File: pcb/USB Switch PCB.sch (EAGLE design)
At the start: 36 parts, among them Q1 2N7002P, Q2 2N7002P, Q3 12 MHz, X1 AMPHENOL-0001LF, X2 UE27-USBA, X3 AMPHENOL-0001LF

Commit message: Starting to look good.
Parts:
- added R10, R11: 100Ω, rcl:R-EU_R0603
- added R7, R8, R9: 12kΩ, rcl:R-EU_R0603
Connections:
- new net GPIO15: MCU.GPIO15, R9.2
- new net GPIO2: MCU.GPIO2, R8.2
- new net N$3: MCU.GPIO5, R10.1
- new net N$5: MCU.GPIO4, R11.1
- net +5V: now also R7.1, R8.1
- net DATAGATE: now also R11.2; no longer MCU.GPIO5
- net GND: now also R9.1
- net GPIO0: now also R7.2
- net POWERGATE: now also R10.2; no longer MCU.GPIO4
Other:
- moved on the sheet: C1, C2, C7, MCU, R3, R4

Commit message: Converting everything
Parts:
- removed C3: 10µF, rcl:C-EUC0603
- removed C4: 100nF, rcl:C-EUC0603
- removed D3: BAS21LT1, USB Switch PCB:BAS40
- removed R5, R6: 470Ω, rcl:R-EU_R0603
- removed U$3: CH340G, ch340g:CH340G
- removed U$4: UMH3N, USB Switch PCB:UMH3N
- removed UIN: (no value), USB Switch PCB:FE05-1
- removed UOUT: (no value), USB Switch PCB:FE04-1
- removed X1, X3: AMPHENOL-0001LF, USB Switch PCB:AMPHENOL-0001LF
- added FLASH, RESET: MOMENTARY-SWITCH, USB Switch PCB:MOMENTARY-SWITCH
- added J1: (no value), SparkFun-Connectors:6_PIN_SERIAL_TARGET
- added U$6: USB-B, USB Switch PCB:USB-B
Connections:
- removed net D+ESP: U$3.D+, X3.D+
- removed net D-ESP: U$3.D-, X3.D-
- removed net DTR: U$3.DTR, U$4.BA, U$4.EB
- removed net ID: UIN.4, X1.ID
- removed net N$4: D3.A, X3.VCC
- removed net N$7: R5.2, U$3.TX
- removed net N$8: R6.2, U$3.RX
- removed net RTS: U$3.RTS, U$4.BB, U$4.EA
- new net ADC: MCU.ADC
- net +3V3: no longer C3.1, C4.1, U$3.VCC
- net +5V: now also J1.VCC; no longer D3.C, U$3.V3
- net D+I: now also U$6.D+; no longer UIN.3, X1.D+
- net D+O: no longer UOUT.3
- net D-I: now also U$6.D-; no longer UIN.2, X1.D-
- net D-O: no longer UOUT.2
- net GND: now also FLASH.P$2, J1.GND, RESET.P$2, U$6.GND; no longer C3.2, C4.2, U$3.GND, UIN.5, X1.GND, X3.GND
- net GNDO: no longer UOUT.4
- net GPIO0: now also FLASH.P$1; no longer U$4.CB
- net RST: now also RESET.P$1; no longer U$4.CA
- net RXD: now also J1.TXO; no longer R6.1
- net TXD: now also J1.RXI; no longer R5.1
- net VCCI: now also U$6.VCC; no longer UIN.1, X1.VCC
- net VCCO: no longer UOUT.1
- net XI: no longer U$3.XI
- net XO: no longer U$3.XO
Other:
- note added: "TODO: Switch to USB B? Current measurement using ADC. Add external GPIO pin access?"
- note removed: "TODO: Switch to USB B Add external ADC and GPIO Add reset circuit Add 3v3 regulator Add weird UMH3N circuit"
- moved on the sheet: C1, C2, C5, C6, C7, MCU, Q3, R10, R11, R3, R4, R7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

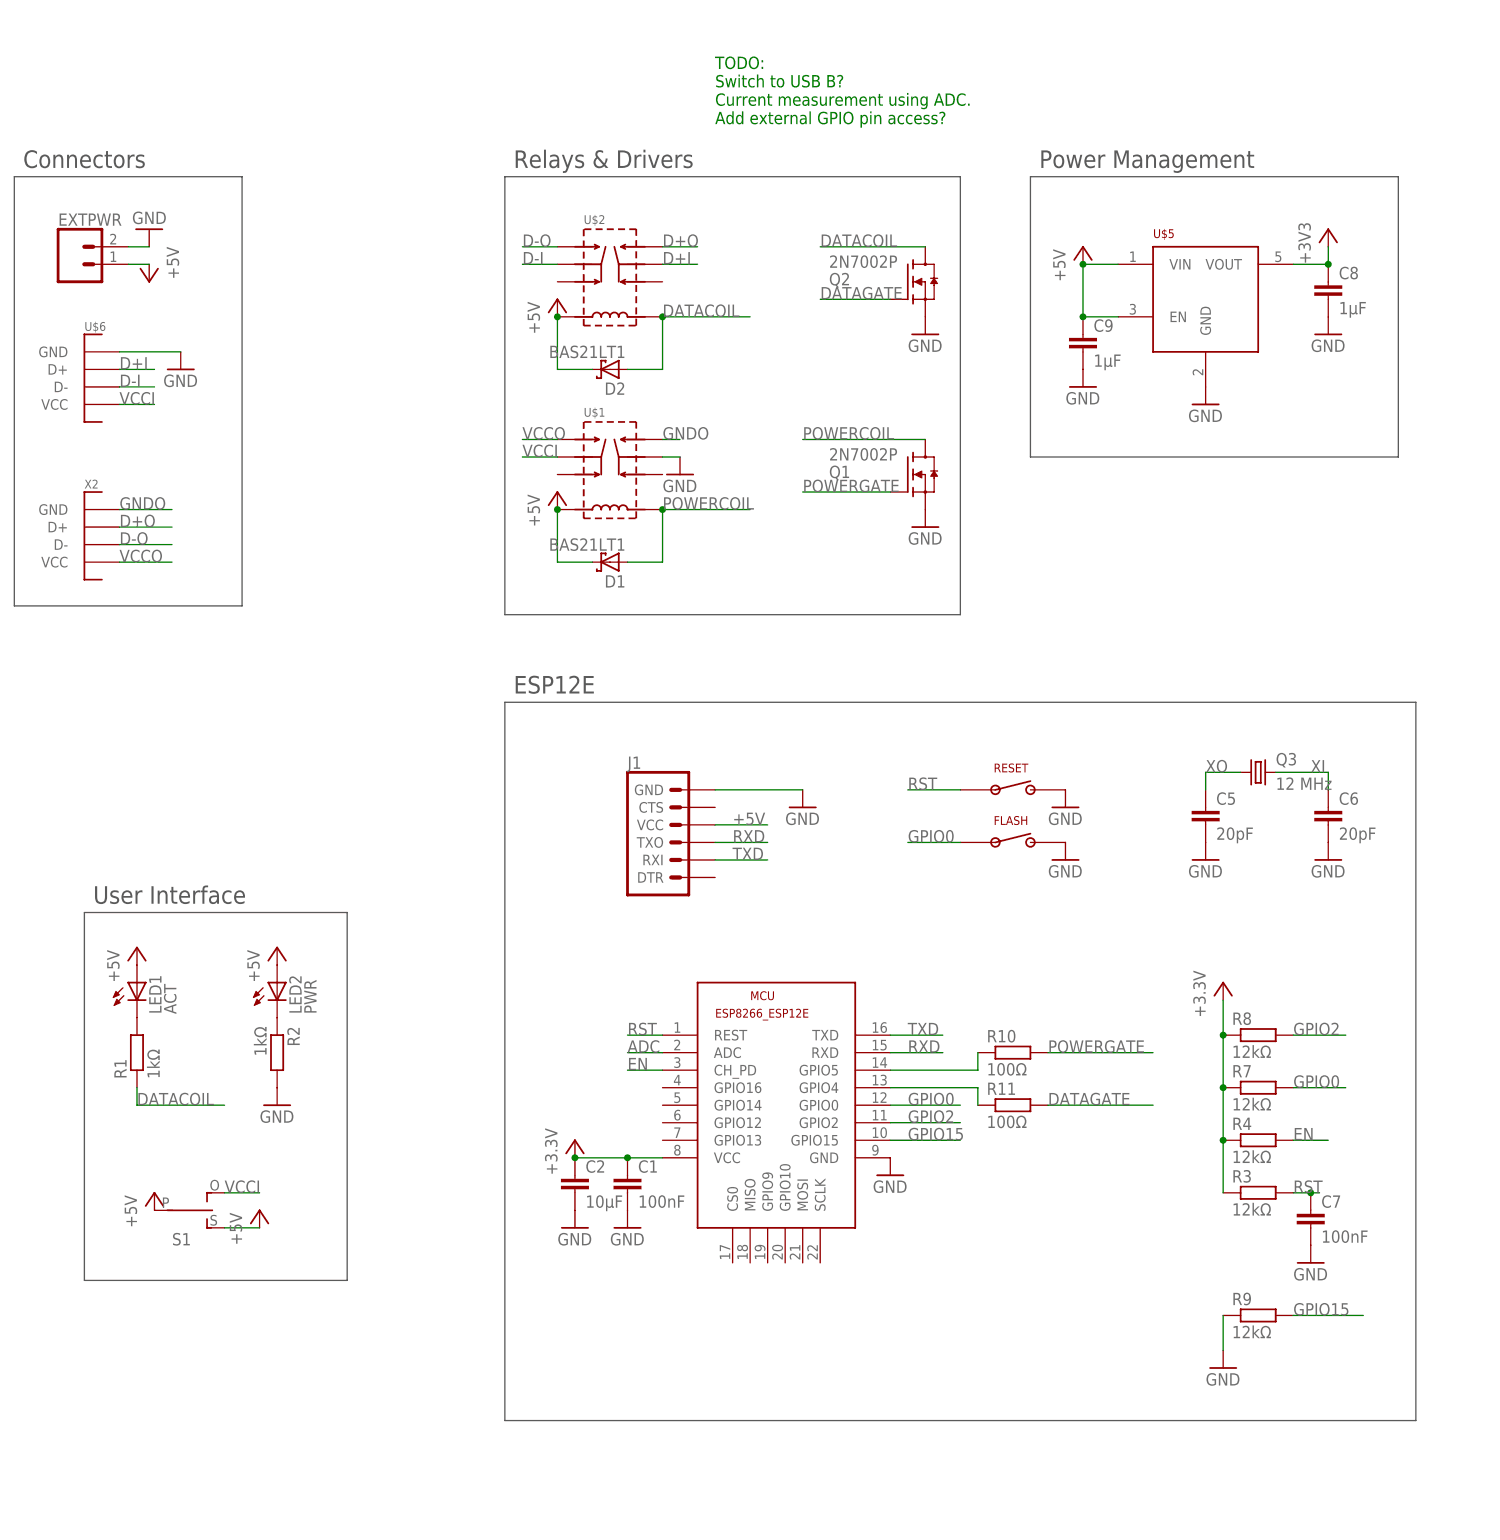
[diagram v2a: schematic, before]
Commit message: Aded momentary switch from banggood.
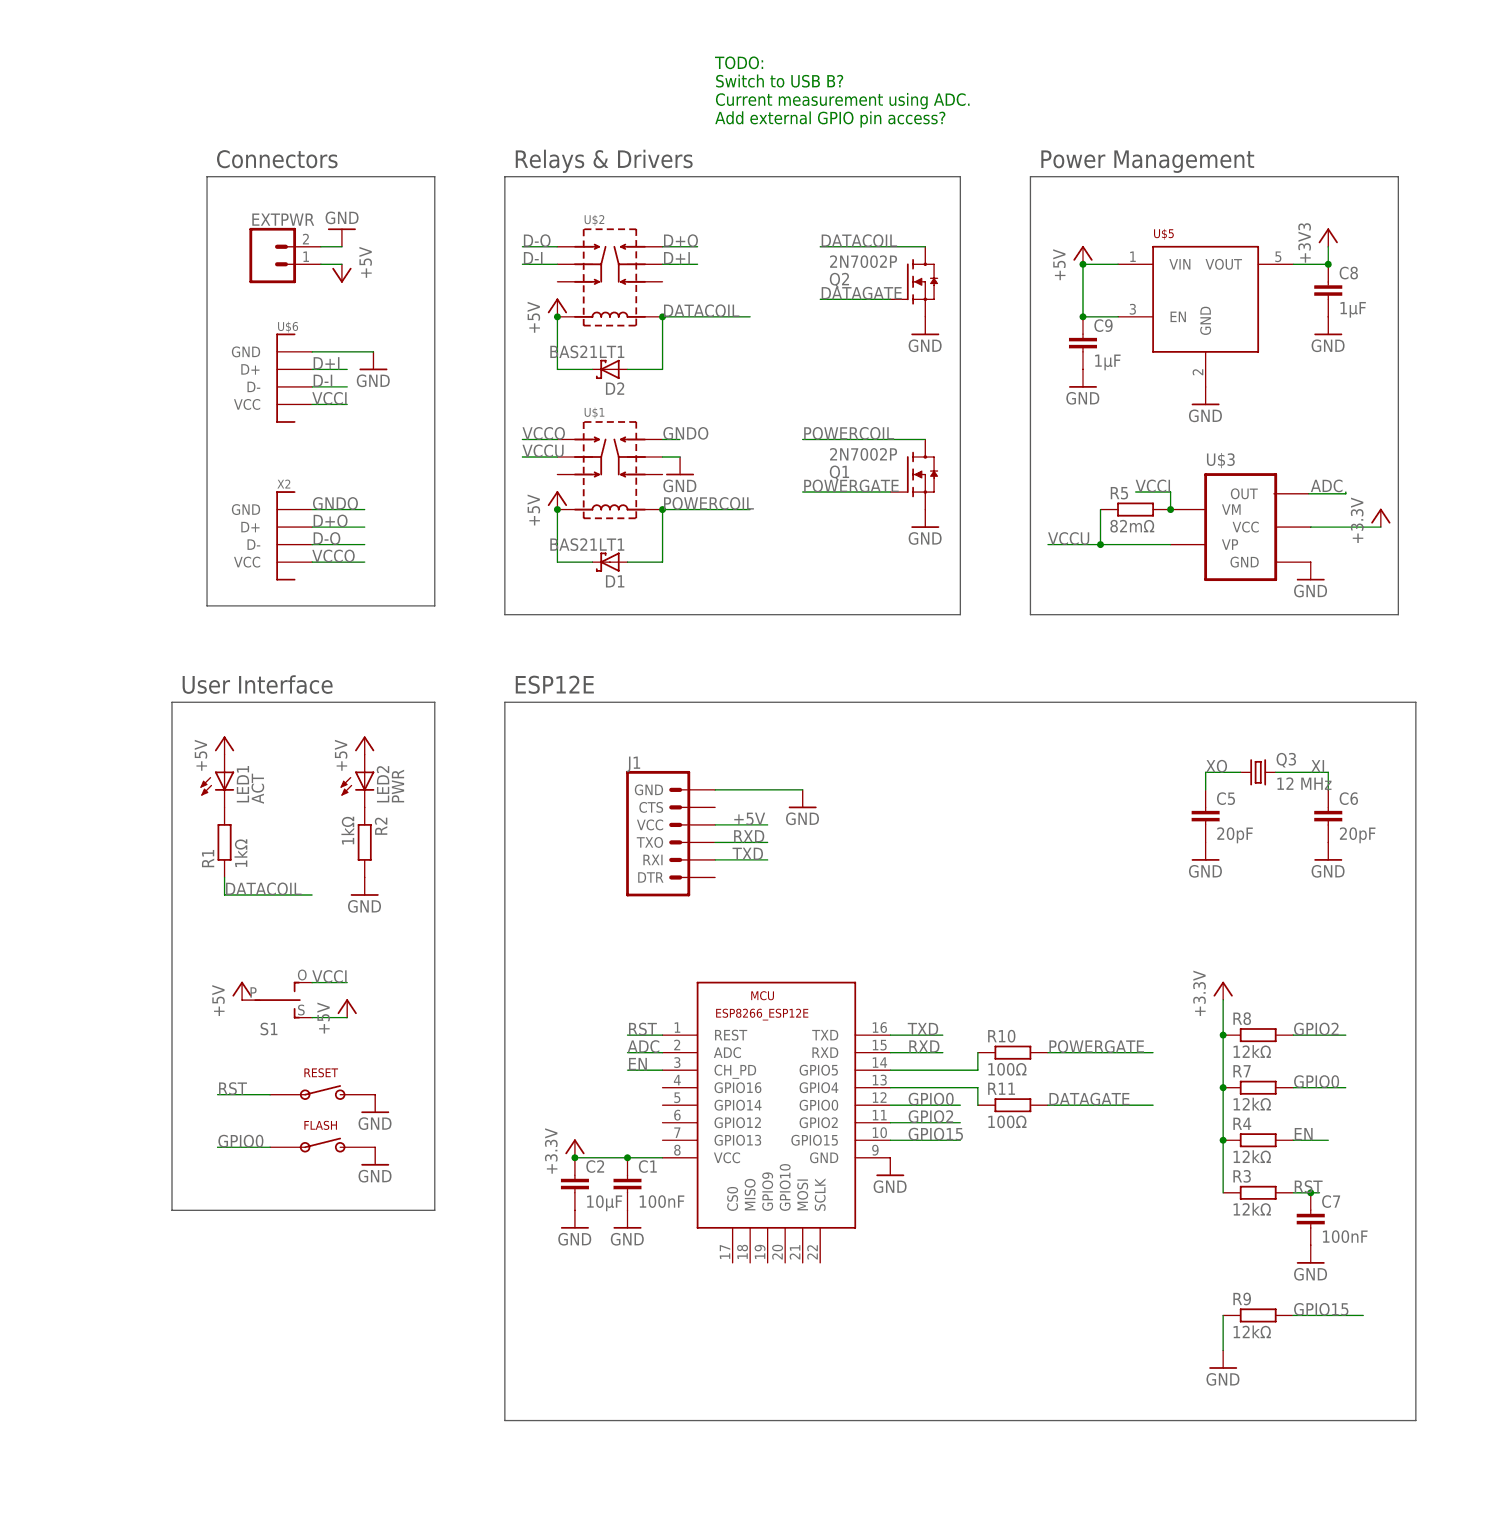
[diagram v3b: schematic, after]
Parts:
- added R5: 82mΩ, rcl:R-EU_R1206
- added U$3: TCS888, USB Switch PCB:TCS888
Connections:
- new net VCCU: R5.1, U$1.C1, U$3.VP
- net +5V: now also U$3.VCC
- net ADC: now also U$3.OUT
- net GND: now also U$3.GND
- net VCCI: now also R5.2, U$3.VM; no longer U$1.C1
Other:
- moved on the sheet: EXTPWR, FLASH, LED1, LED2, R1, R2, RESET, S1, U$6, X2

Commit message: Current measurement circuit now done.
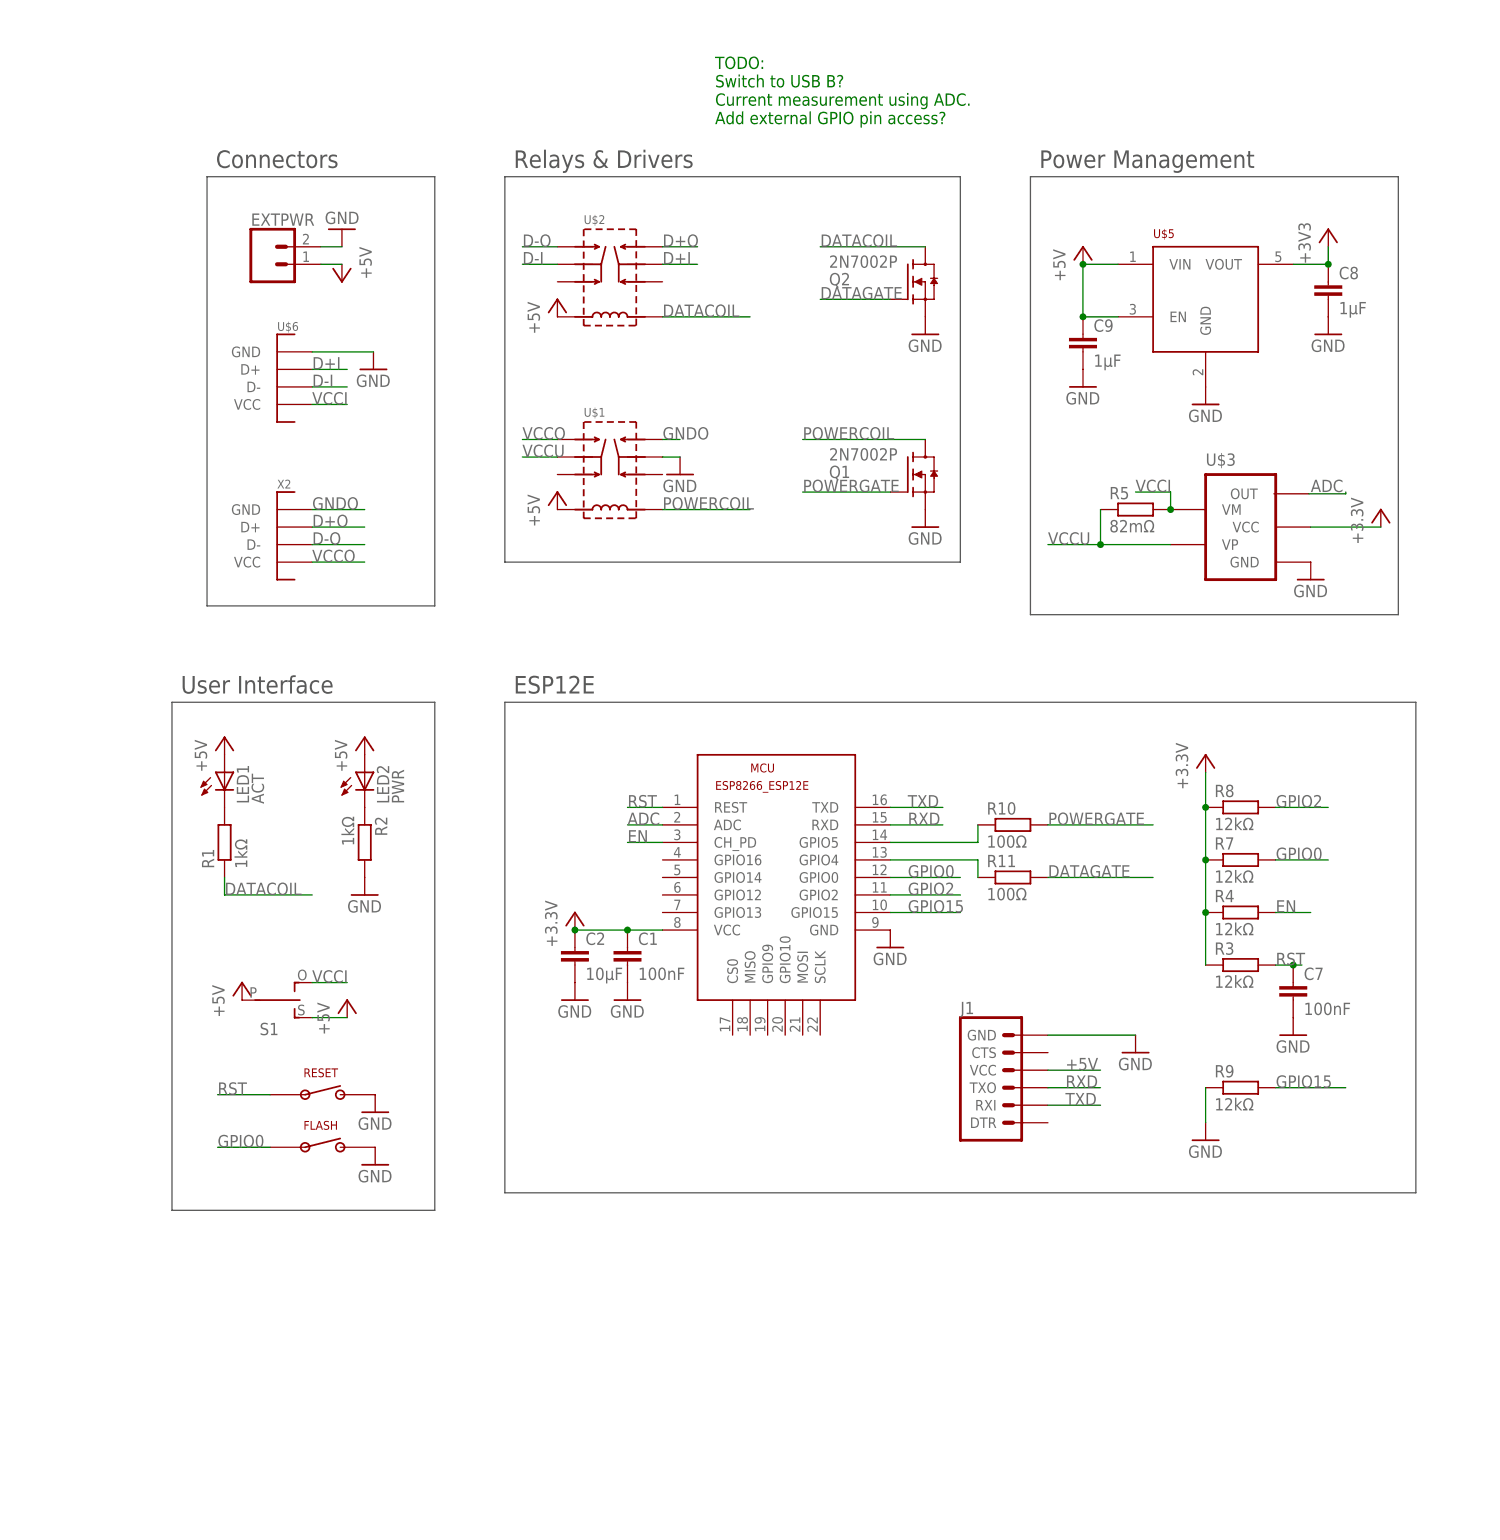
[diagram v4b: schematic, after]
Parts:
- removed C5, C6: 20pF, rcl:C-EUC0603
- removed D1, D2: BAS21LT1, USB Switch PCB:BAS40
- removed Q3: 12 MHz, USB Switch PCB:CSM-3XCSM-3X
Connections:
- removed net XI: C6.1, Q3.2
- removed net XO: C5.1, Q3.1
- net +5V: no longer D1.C, D2.C
- net DATACOIL: no longer D2.A
- net GND: no longer C5.2, C6.2
- net POWERCOIL: no longer D1.A
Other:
- moved on the sheet: C1, C2, C7, J1, MCU, R10, R11, R3, R4, R7, R8, R9
